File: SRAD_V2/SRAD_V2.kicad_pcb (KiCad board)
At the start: 4 copper layers, 37 parts, among them IC1 NCV81071BZR2G, IC2 NCV81071BZR2G, J1 DC Jack, J2 691210910002, J3 691210910002, J4 691210910002, J5 691210910002, M1 FDC8878, Q1 AOSP36326C, Q2 AOSP36326C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

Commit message: more changes
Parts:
- removed M1: FDC8878, FDC8878:SuperSot6_SOT-23-6_1P6X2P9_ONS
- removed Q5: FDD1600N10ALZ, FDD1600N10ALZ:TO252_FDD1600_ONS-L
- moved C4 94.0 mm to (60.2, 67.0)
- moved C5 94.0 mm to (60.2, 69.5)
- moved C6 94.0 mm to (60.2, 72.0)
- moved LED1 90.5 mm to (46.0, 95.8)
- moved J1 87.5 mm to (58.2, 51.9)
- moved Q1 87.3 mm to (42.5, 64.1)
- moved Q2 87.3 mm to (42.5, 71.0)
- moved Q3 87.3 mm to (42.5, 77.9)
- moved Q4 87.3 mm to (42.5, 84.8)
- moved CR1 79.9 mm to (81.3, 48.5)
- moved CR2 79.9 mm to (81.3, 51.3)
- moved CR3 79.9 mm to (81.3, 54.1)
- moved CR4 79.9 mm to (81.3, 56.9)
- moved C2 79.2 mm to (58.9, 155.2)
- moved C3 79.2 mm to (58.9, 158.2)
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
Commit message: finalish changes
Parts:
- removed U1: STM32F767ZIT6, STM32F767ZIT6:LQFP144-20x20mm_STM
- removed U10: AS5F31G04SND-08LIN, NAND_Flash:SON127P600X800X80-8N
- removed U5: MAX-M10S, RF_GPS:ublox_MAX
- removed U6: MS5607-02BA, Package_LGA:LGA-8_3x5mm_P1.25mm
- removed U9: MCP9808_DFN, Package_DFN_QFN:DFN-8-1EP_3x2mm_P0.5mm_EP1.7x1.4mm
- added M1: FDC8878, FDC8878:SuperSot6_SOT-23-6_1P6X2P9_ONS, F.Cu at (180.4, 102.0)
- added Q5: FDD1600N10ALZ, FDD1600N10ALZ:TO252_FDD1600_ONS-L, F.Cu at (177.5, 83.6)
- added U12: MAX-M10S, RF_GPS:ublox_MAX, F.Cu at (129.0, 100.6)
- added U13: MS5607-02BA, Package_LGA:LGA-8_3x5mm_P1.25mm, F.Cu at (149.1, 98.2)
- added U16: MCP9808_DFN, Package_DFN_QFN:DFN-8-1EP_3x2mm_P0.5mm_EP1.7x1.4mm, F.Cu at (138.3, 104.1)
- added U17: AS5F31G04SND-08LIN, NAND_Flash:SON127P600X800X80-8N, F.Cu at (141.5, 98.5)
- added U4: STM32F767ZIT6, STM32F767ZIT6:LQFP144-20x20mm_STM, F.Cu at (135.0, 82.4)
- moved C4 123.9 mm to (183.5, 79.5)
- moved C5 123.9 mm to (183.5, 82.0)
- moved C6 123.9 mm to (183.5, 84.5)
- moved LED1 120.7 mm to (166.4, 104.4)
- moved Q1 116.6 mm to (157.7, 81.8)
- moved Q2 116.6 mm to (157.7, 88.8)
- moved Q3 116.6 mm to (157.7, 95.7)
- moved Q4 116.6 mm to (157.7, 102.6)
- moved J1 114.3 mm to (167.2, 86.2)
- moved C1 109.5 mm to (159.6, 109.4)
- moved C2 109.5 mm to (159.6, 112.4)
- moved C3 109.5 mm to (159.6, 115.4)
- moved R1 109.5 mm to (158.9, 117.9)
- moved Cout2 109.5 mm to (155.4, 111.7)
- moved Cout3 109.5 mm to (155.4, 114.2)
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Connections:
- net /E-match Firing Circuit/Sensor_Output renamed /E-match Firing Circuit/IVAL
- net /E-match Firing Circuit/Trigger_Signal1 renamed /E-match Firing Circuit/CH1
- net /E-match Firing Circuit/Trigger_Signal2 renamed /E-match Firing Circuit/CH2
- net /E-match Firing Circuit/Trigger_Signal3 renamed /E-match Firing Circuit/CH3
- net /E-match Firing Circuit/Trigger_Signal4 renamed /E-match Firing Circuit/CH4
- net /Power Delivery System/V3V3 renamed /Power Delivery System/+3V3
- net VBAT renamed /E-match Firing Circuit/VBAT
- IC1 pad 1: /E-match Firing Circuit/Enable_Signal3 -> unconnected-(IC1-ENA-Pad1)
- IC1 pad 3: /E-match Firing Circuit/Enable_Signal4 -> unconnected-(IC1-ENB-Pad3)
- IC2 pad 1: /E-match Firing Circuit/Enable_Signal1 -> unconnected-(IC2-ENA-Pad1)
- IC2 pad 3: /E-match Firing Circuit/Enable_Signal2 -> unconnected-(IC2-ENB-Pad3)

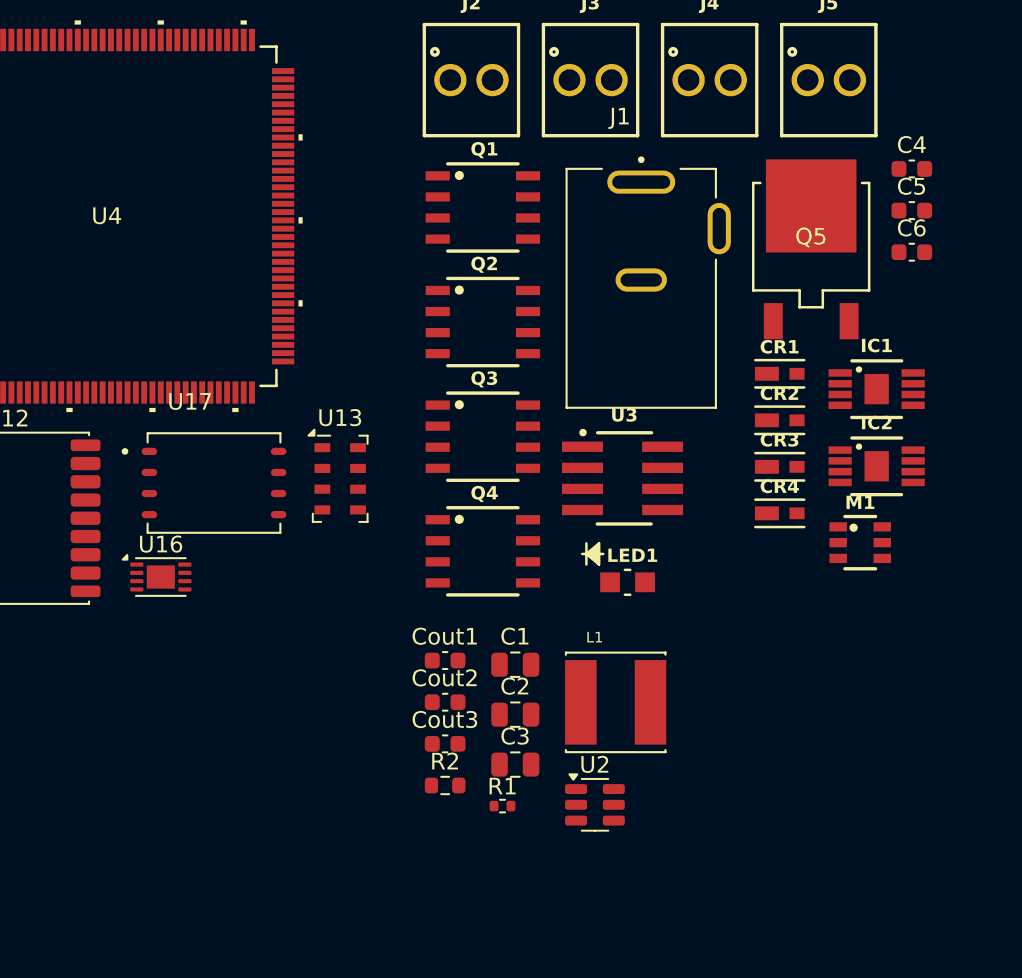
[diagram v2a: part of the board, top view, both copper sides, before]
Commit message: new connector
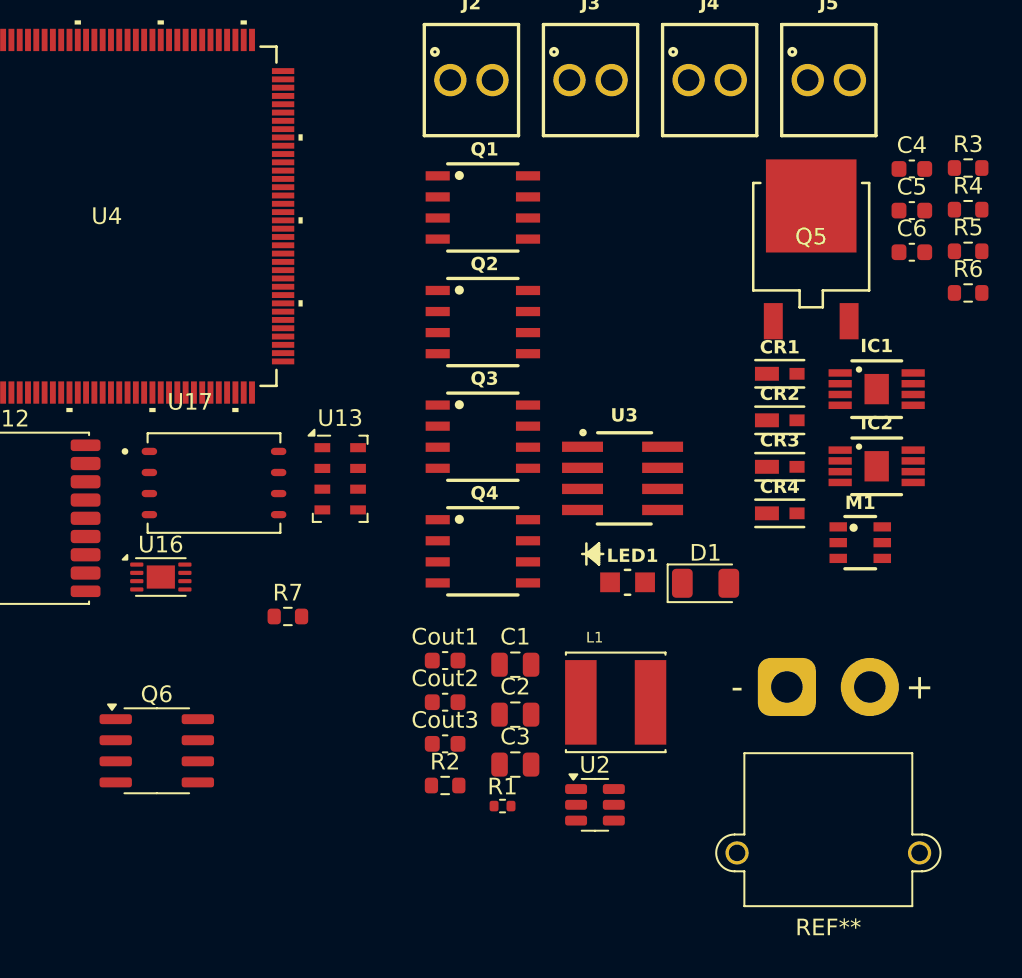
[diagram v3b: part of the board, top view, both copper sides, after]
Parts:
- removed J1: DC Jack, DC-Jack:TENSILITY_54-00130
- added D1: IR26-21C_L110_TR8, LED_SMD:LED_1206_3216Metric, F.Cu at (171.1, 104.5)
- added Q6: FDS6630A, Package_SO:SOIC-8_3.9x4.9mm_P1.27mm, F.Cu at (138.0, 114.6)
- added R3: 10R, Resistor_SMD:R_0603_1608Metric, F.Cu at (186.9, 79.5)
- added R4: 10R, Resistor_SMD:R_0603_1608Metric, F.Cu at (186.9, 82.0)
- added R5: 10R, Resistor_SMD:R_0603_1608Metric, F.Cu at (186.9, 84.5)
- added R6: 10R, Resistor_SMD:R_0603_1608Metric, F.Cu at (186.9, 87.0)
- added R7: 330R, Resistor_SMD:R_0603_1608Metric, F.Cu at (145.9, 106.5)
- added REF**: AMASS_XT30PW-M_1x02_P2.50mm_Horizontal, Connector_AMASS:AMASS_XT30PW-M_1x02_P2.50mm_Horizontal, F.Cu at (176.0, 110.8)

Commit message: tinkered with the layout
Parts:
- removed Q5: FDD1600N10ALZ, FDD1600N10ALZ:TO252_FDD1600_ONS-L
- added REF**: MountingHole_2.2mm_M2_DIN965_Pad_TopBottom, MountingHole:MountingHole_2.2mm_M2_DIN965_Pad_TopBottom, F.Cu at (210.0, 50.0)
- added REF**: MountingHole_2.2mm_M2_DIN965_Pad_TopBottom, MountingHole:MountingHole_2.2mm_M2_DIN965_Pad_TopBottom, F.Cu at (210.0, 145.0)
- added REF**: MountingHole_2.2mm_M2_DIN965_Pad_TopBottom, MountingHole:MountingHole_2.2mm_M2_DIN965_Pad_TopBottom, F.Cu at (170.0, 50.0)
- added REF**: MountingHole_2.2mm_M2_DIN965_Pad_TopBottom, MountingHole:MountingHole_2.2mm_M2_DIN965_Pad_TopBottom, F.Cu at (170.0, 145.0)
- moved U16 66.0 mm to (196.3, 135.5)
- moved U4 65.2 mm to (194.6, 108.8)
- moved Q6 63.6 mm to (194.5, 143.8)
- moved R7 63.6 mm to (202.4, 135.8)
- moved U12 63.6 mm to (185.5, 129.8)
- moved U13 63.6 mm to (205.6, 127.5)
- moved U17 63.6 mm to (198.0, 127.7)
- moved REF** 54.9 mm to (193.5, 58.8), turned to 0 degrees
- moved J2 49.8 mm to (202.7, 54.3), turned to -90 degrees
- moved J3 40.6 mm to (202.7, 61.5), turned to -90 degrees
- moved Cout2 40.0 mm to (185.6, 85.4)
- moved U2 40.0 mm to (194.6, 91.5)
- moved C2 40.0 mm to (189.8, 86.1)
- moved Cout1 40.0 mm to (185.6, 82.9)
- moved Cout3 40.0 mm to (185.6, 87.9)
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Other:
- board outline added: 50 x 105 mm

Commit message: added text-box for communication protocols in the schematic
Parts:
- added Q5: RQ6E080AJ, Package_TO_SOT_SMD:SOT-23-6, F.Cu at (211.2, 80.8)
- added kibuzzard-69B6CF6F: G***, kibuzzard-69B6CF6F, F.Cu at (185.0, 140.8)
- added kibuzzard-69B6CF86: G***, kibuzzard-69B6CF86, F.Cu at (199.1, 140.8)
- added kibuzzard-69B6E669: G***, kibuzzard-69B6E669, F.Cu at (191.8, 144.0)
- moved Q6 33.9 mm to (172.5, 118.1)

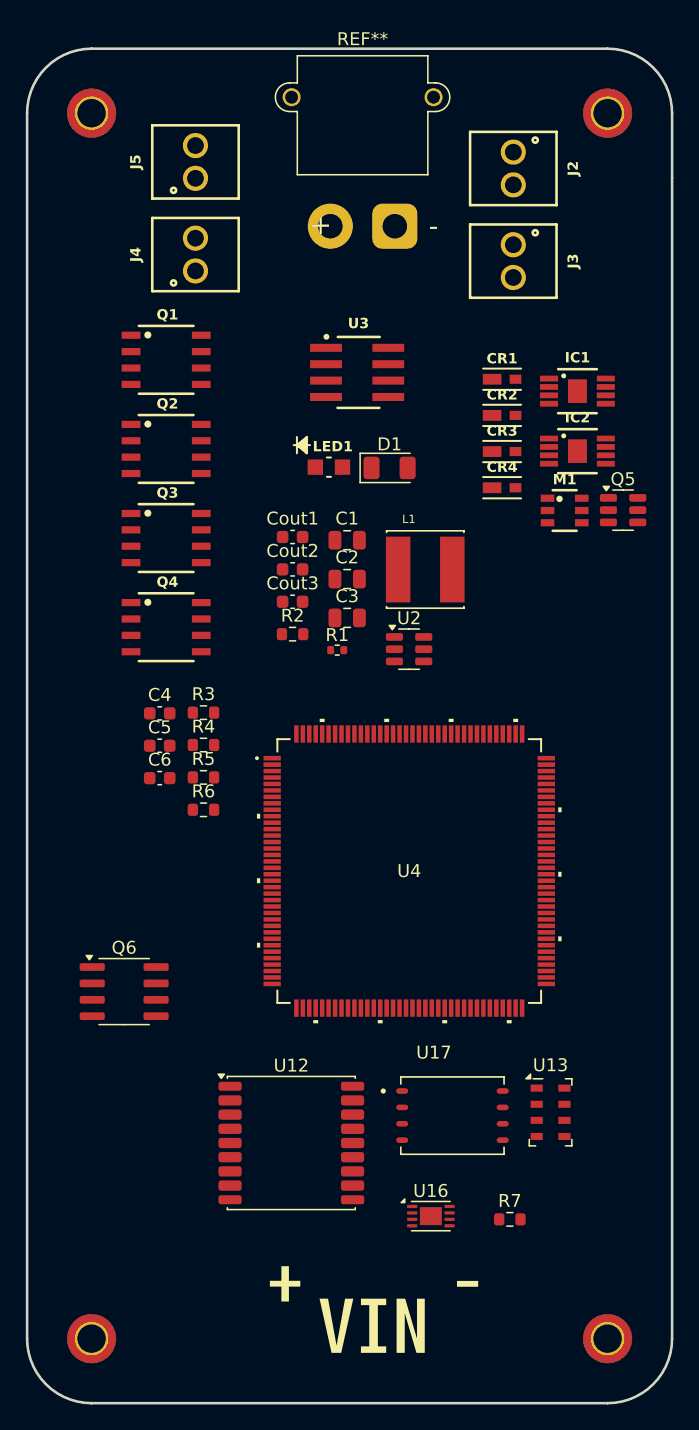
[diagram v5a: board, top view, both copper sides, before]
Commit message: added bunch of decoupling capacitors, updated mosfet symbols with KICAD in-built ones etc
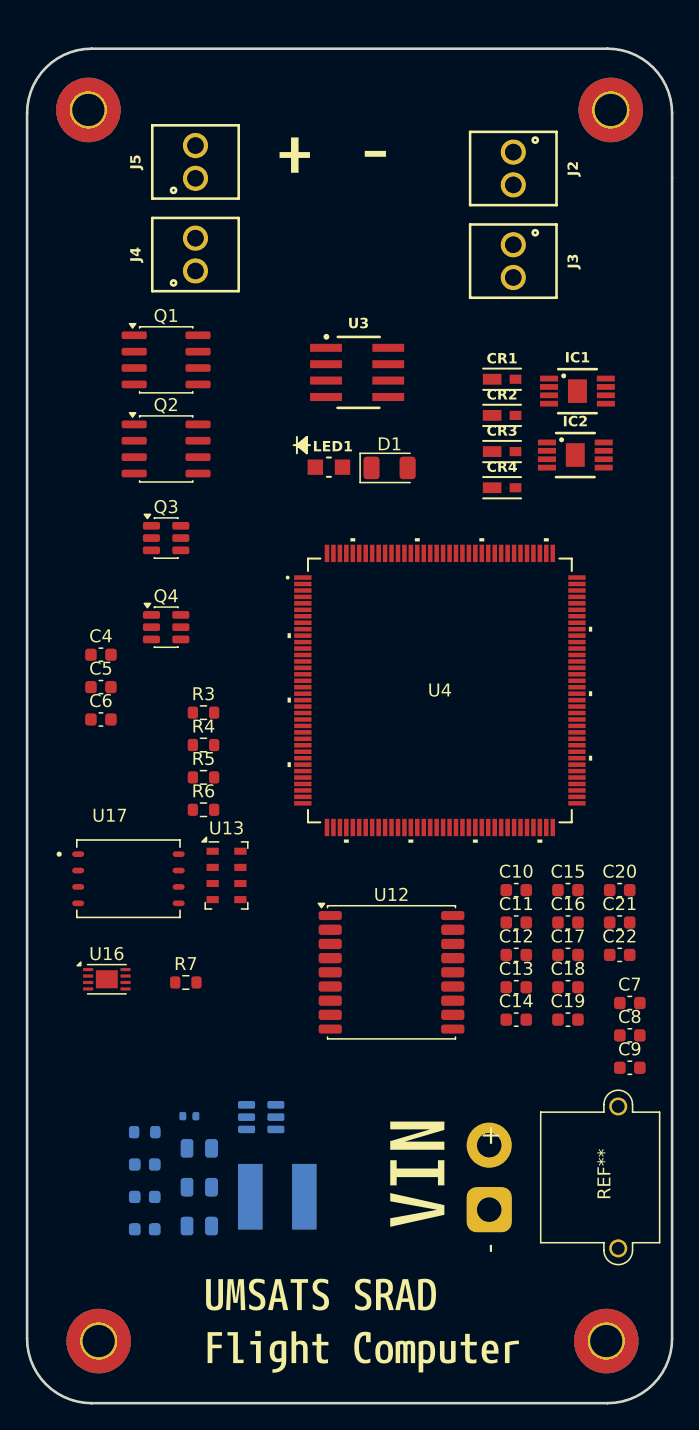
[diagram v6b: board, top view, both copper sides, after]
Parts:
- removed M1: FDC8878, FDC8878:SuperSot6_SOT-23-6_1P6X2P9_ONS
- removed Q5: RQ6E080AJ, Package_TO_SOT_SMD:SOT-23-6
- removed Q6: FDS6630A, Package_SO:SOIC-8_3.9x4.9mm_P1.27mm
- removed the REF** at (210.0, 50.0)
- removed the REF** at (210.0, 145.0)
- removed the REF** at (170.0, 50.0)
- removed the REF** at (170.0, 145.0)
- added C10: 10u, Capacitor_SMD:C_0603_1608Metric, F.Cu at (202.9, 110.2)
- added C11: 0.1u, Capacitor_SMD:C_0603_1608Metric, F.Cu at (202.9, 112.7)
- added C12: 0.1u, Capacitor_SMD:C_0603_1608Metric, F.Cu at (202.9, 115.2)
- added C13: 0.1u, Capacitor_SMD:C_0603_1608Metric, F.Cu at (202.9, 117.8)
- added C14: 10u, Capacitor_SMD:C_0603_1608Metric, F.Cu at (202.9, 120.3)
- added C15: 10u, Capacitor_SMD:C_0603_1608Metric, F.Cu at (206.9, 110.2)
- added C16: 0.1u, Capacitor_SMD:C_0603_1608Metric, F.Cu at (206.9, 112.7)
- added C17: 10u, Capacitor_SMD:C_0603_1608Metric, F.Cu at (206.9, 115.2)
- added C18: 0.1u, Capacitor_SMD:C_0603_1608Metric, F.Cu at (206.9, 117.8)
- added C19: 0.1u, Capacitor_SMD:C_0603_1608Metric, F.Cu at (206.9, 120.3)
- added C20: 10u, Capacitor_SMD:C_0603_1608Metric, F.Cu at (210.9, 110.2)
- added C21: 0.1u, Capacitor_SMD:C_0603_1608Metric, F.Cu at (210.9, 112.7)
- added C22: 10u, Capacitor_SMD:C_0603_1608Metric, F.Cu at (210.9, 115.2)
- added C7: 0.1u, Capacitor_SMD:C_0603_1608Metric, F.Cu at (211.7, 119.0)
- added C8: 0.1u, Capacitor_SMD:C_0603_1608Metric, F.Cu at (211.7, 121.5)
- added C9: 0.1u, Capacitor_SMD:C_0603_1608Metric, F.Cu at (211.7, 124.0)
- added REF**: MountingHole_2.5mm_Pad_TopBottom, MountingHole:MountingHole_2.5mm_Pad_TopBottom, F.Cu at (170.6, 145.2)
- added REF**: MountingHole_2.5mm_Pad_TopBottom, MountingHole:MountingHole_2.5mm_Pad_TopBottom, F.Cu at (210.2, 49.8)
- added REF**: MountingHole_2.5mm_Pad_TopBottom, MountingHole:MountingHole_2.5mm_Pad_TopBottom, F.Cu at (169.8, 49.8)
- added REF**: MountingHole_2.5mm_Pad_TopBottom, MountingHole:MountingHole_2.5mm_Pad_TopBottom, F.Cu at (209.9, 145.2)
- added kibuzzard-69B89FDF: G***, kibuzzard-69B89FDF, F.Cu at (191.0, 144.0)
- C1, C2, C3, Cout1, Cout2, Cout3, L1, R1, R2, U2: moved to B.Cu
- C4, C5, C6: value C_Small -> 10u
- Q1, Q2: value AOSP36326C -> FDS6630A; footprint AOSP36326C:SO8SOP-8L_AOS -> Package_SO:SOIC-8_3.9x4.9mm_P1.27mm
- Q3, Q4: value AOSP36326C -> RQ6E080AJ; footprint AOSP36326C:SO8SOP-8L_AOS -> Package_TO_SOT_SMD:SOT-23-6
- moved kibuzzard-69B6CF86 87.9 mm to (192.0, 53.1)
- moved kibuzzard-69B6CF6F 87.5 mm to (185.8, 53.2)
- moved REF** 76.6 mm to (200.8, 135.0), turned to -90 degrees
- moved Cout1 54.9 mm to (174.1, 136.5)
- moved C1 54.4 mm to (178.3, 136.3)
- moved Cout2 50.0 mm to (174.1, 134.0)
- moved L1 50.0 mm to (184.4, 134.0)
- moved C2 48.5 mm to (178.3, 133.3)
- moved Cout3 45.1 mm to (174.1, 131.5)
- moved C3 42.7 mm to (178.3, 130.2)
- moved R2 40.3 mm to (174.1, 129.0)
- moved U2 38.0 mm to (183.2, 127.8)
- moved R1 37.9 mm to (177.6, 127.8)
- moved R7 31.1 mm to (177.3, 117.4)
- moved U16 31.1 mm to (171.2, 117.1)
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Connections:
- Q3 pad 1: GND -> Net-(CR3-Pad2)
- Q3 pad 2: GND -> Net-(CR3-Pad2)
- Q3 pad 3: GND -> Net-(Q3-G)
- Q3 pad 4: Net-(Q3-Pad4) -> GND
- Q4 pad 1: GND -> Net-(CR4-Pad2)
- Q4 pad 2: GND -> Net-(CR4-Pad2)
- Q4 pad 3: GND -> Net-(Q4-G)
- Q4 pad 4: Net-(Q4-Pad4) -> GND
- R5 pad 1: Net-(Q3-Pad4) -> Net-(Q3-G)
- R6 pad 1: Net-(Q4-Pad4) -> Net-(Q4-G)

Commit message: fixed some origin issues on pcb -- working on the PDS
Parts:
- added Cout4: 0.1uF, Capacitor_SMD:C_0603_1608Metric, F.Cu at (120.0, 101.7)
- C1, C2, C3, Cout1, Cout2, Cout3, L1, R1, R2, U2: moved to F.Cu
- moved Cout3 74.0 mm to (116.5, 85.0), turned to 180 degrees
- moved C1 73.9 mm to (113.0, 101.7), turned to 90 degrees
- moved Cout2 73.7 mm to (116.5, 88.0), turned to 180 degrees
- moved Cout1 73.4 mm to (116.5, 91.0), turned to 180 degrees
- moved C2 69.4 mm to (116.5, 101.7), turned to 90 degrees
- moved L1 69.0 mm to (128.5, 93.5), turned to 90 degrees
- moved U2 63.0 mm to (126.4, 100.5)
- moved R1 53.4 mm to (128.0, 108.0)
- moved C3 50.6 mm to (137.0, 101.0), turned to -90 degrees
- moved R2 49.8 mm to (131.7, 103.0)
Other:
- board size 50 x 105 mm -> 115 x 105 mm

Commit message: PDS pcb layout
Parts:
- added kibuzzard-69BEBA35: G***, kibuzzard-69BEBA35, F.Cu at (113.4, 96.5)
- added kibuzzard-69BEBA60: G***, kibuzzard-69BEBA60, F.Cu at (117.2, 105.6)
- moved L1 1.12 mm to (128.0, 92.5)
- moved C1 0.28 mm to (113.0, 102.0)
- moved C2 0.28 mm to (116.5, 102.0)
- moved Cout4 0.28 mm to (120.0, 102.0)
- moved R2 0.18 mm to (131.5, 103.0)
- moved U2 0.15 mm to (126.5, 100.5)
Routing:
- added copper zone on F.Cu, net /Power Delivery System/VIN
- added copper zone on F.Cu, net GND
